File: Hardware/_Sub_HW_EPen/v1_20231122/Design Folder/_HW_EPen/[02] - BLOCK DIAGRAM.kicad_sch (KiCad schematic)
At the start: 0 parts

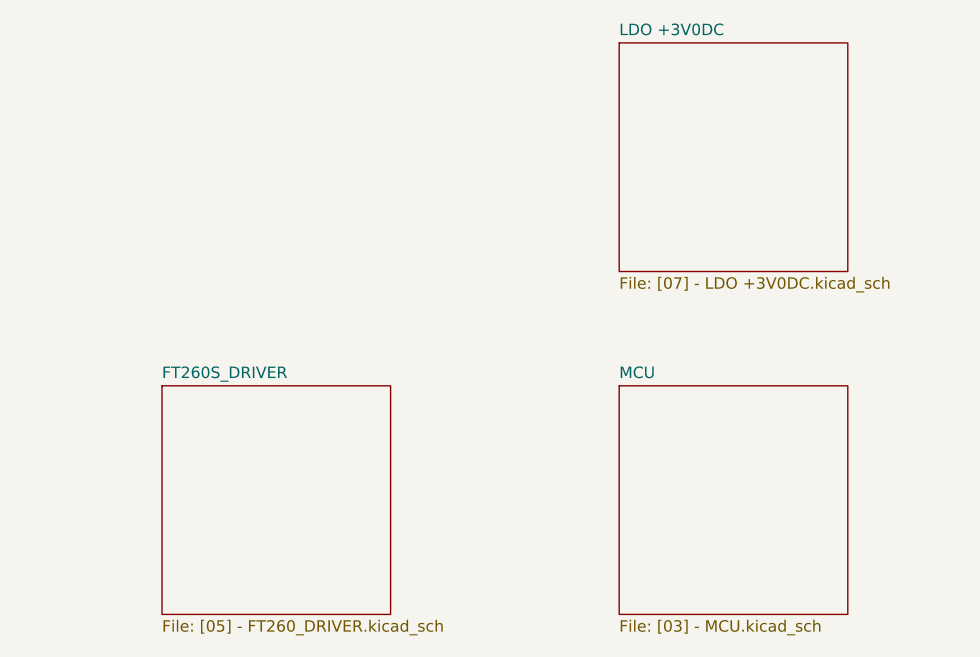
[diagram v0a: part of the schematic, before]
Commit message: Working on EPen schematic
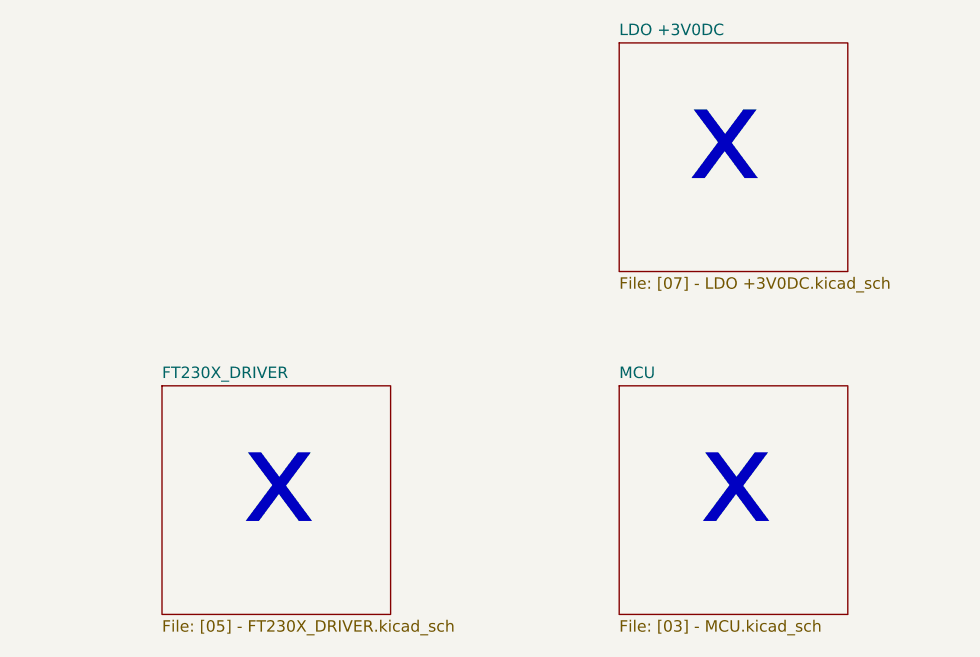
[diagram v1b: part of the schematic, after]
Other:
- sheet FT260S_DRIVER renamed FT230X_DRIVER
- sheet FT230X_DRIVER: file [05] - FT260_DRIVER.kicad_sch -> [05] - FT230X_DRIVER.kicad_sch
- note added: "x"
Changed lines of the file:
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@@
 (kicad_sch (version 20230121) (generator eeschema)
   (paper "B")
+  (text "x" (at 199.39 143.51 0)
+    (effects (font (size 10.16 10.16)) (justify left bottom))
+  )
+  (text "x" (at 148.59 143.51 0)
+    (effects (font (size 10.16 10.16)) (justify left bottom))
+  )
+  (text "x" (at 198.12 105.41 0)
+    (effects (font (size 10.16 10.16)) (justify left bottom))
+  )
   (sheet (at 88.9 127) (size 25.4 25.4) (fields_autoplaced)
     (stroke (width 0.1524) (type solid))
@@
     (stroke (width 0.1524) (type solid))
     (fill (color 0 0 0 0.0000))
-    (property "Sheetname" "FT260S_DRIVER" (at 139.7 126.2884 0)
+    (property "Sheetname" "FT230X_DRIVER" (at 139.7 126.2884 0)
       (effects (font (size 1.27 1.27)) (justify left bottom))
     )
-    (property "Sheetfile" "[05] - FT260_DRIVER.kicad_sch" (at 139.7 152.9846 0)
+    (property "Sheetfile" "[05] - FT230X_DRIVER.kicad_sch" (at 139.7 152.9846 0)
       (effects (font (size 1.27 1.27)) (justify left top))
     )

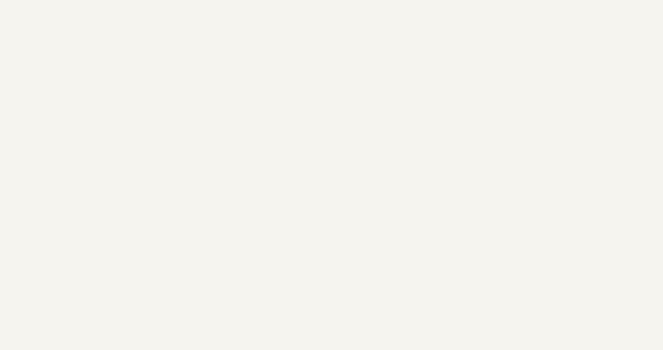
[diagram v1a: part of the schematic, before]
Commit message: Working on EPen schematic
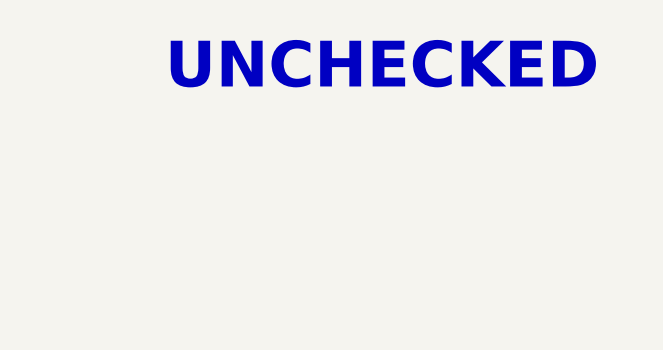
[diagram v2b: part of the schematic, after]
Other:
- note added: "UNCHECKED"
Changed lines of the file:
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@@
 (kicad_sch (version 20230121) (generator eeschema)
   (paper "B")
+  (text "UNCHECKED" (at 369.57 36.83 0)
+    (effects (font (size 5.08 5.08) (thickness 1.016) bold) (justify left bottom))
+  )
   (text "x" (at 199.39 143.51 0)
     (effects (font (size 10.16 10.16)) (justify left bottom))

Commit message: Working on Epen Schematic
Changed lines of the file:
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@@
     (effects (font (size 5.08 5.08) (thickness 1.016) bold) (justify left bottom))
   )
-  (text "x" (at 199.39 143.51 0)
+  (text "x" (at 248.92 143.51 0)
     (effects (font (size 10.16 10.16)) (justify left bottom))
   )
@@
     (effects (font (size 10.16 10.16)) (justify left bottom))
   )
+  (text "x" (at 96.52 143.51 0)
+    (effects (font (size 10.16 10.16)) (justify left bottom))
+  )

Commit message: More progress on EPen Hardware
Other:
- sheet FT230X_DRIVER ports: added UART_RX, UART_TX, USBDM, USBDP, VIN; removed none
- sheet LDO +3V0DC ports: added +3VOUT, MIC5365_EN, VIN; removed none
- sheet MCU ports: added BUFF_~{EN}, EEPROM_~{WP}, MCU_~{RESET}, MIC5365_EN, SPI_CLK, SPI_CS, SPI_MISO, SPI_MOSI, UART_RX, UART_TX, VIN; removed none
- sheet OUTPUT ports: added A1, A2, A4, A5, A6, VIN, Y3, ~{EN}; removed none
- sheet USB ports: added USBDM, USBDP, VBUS; removed none
- note removed: "UNCHECKED"
- note removed: "x"
- company: (none) -> mend0z0
- title: (none) -> EPen
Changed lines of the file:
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@@
 (kicad_sch (version 20230121) (generator eeschema)
   (paper "B")
-  (text "UNCHECKED" (at 369.57 36.83 0)
-    (effects (font (size 5.08 5.08) (thickness 1.016) bold) (justify left bottom))
-  )
-  (text "x" (at 248.92 143.51 0)
-    (effects (font (size 10.16 10.16)) (justify left bottom))
-  )
-  (text "x" (at 148.59 143.51 0)
-    (effects (font (size 10.16 10.16)) (justify left bottom))
-  )
-  (text "x" (at 198.12 105.41 0)
-    (effects (font (size 10.16 10.16)) (justify left bottom))
-  )
-  (text "x" (at 96.52 143.51 0)
-    (effects (font (size 10.16 10.16)) (justify left bottom))
+  (title_block
+    (title "EPen")
+    (date "2023-11-27")
+    (rev "v1.0")
+    (company "mend0z0")
+    (comment 1 "v1.0")
+    (comment 2 "PRELIMINARY")
+    (comment 4 "_BOM_EPen.html")
+    (comment 5 "_HW_EPen.pcb")
+    (comment 6 "_GBR_EPen.zip")
+    (comment 7 "_BOM_EPen.html")
+    (comment 9 "First Release")
+  )
+  (junction (at 177.8 93.98) (diameter 0) (color 0 0 0 0)
+  )
+  (junction (at 127 130.81) (diameter 0) (color 0 0 0 0)
+  )
+  (wire (pts (xy 215.9 138.43) (xy 266.7 138.43))
+    (stroke (width 0) (type default))
+  )
+  (wire (pts (xy 215.9 140.97) (xy 266.7 140.97))
+    (stroke (width 0) (type default))
+  )
+  (wire (pts (xy 222.25 129.54) (xy 222.25 106.68))
+    (stroke (width 0) (type default))
+  )
+  (wire (pts (xy 114.3 138.43) (xy 139.7 138.43))
+    (stroke (width 0) (type default))
+  )
+  (wire (pts (xy 190.5 129.54) (xy 177.8 129.54))
+    (stroke (width 0) (type default))
+  )
+  (wire (pts (xy 127 130.81) (xy 139.7 130.81))
+    (stroke (width 0) (type default))
+  )
+  (wire (pts (xy 215.9 135.89) (xy 266.7 135.89))
+    (stroke (width 0) (type default))
+  )
+  (wire (pts (xy 165.1 140.97) (xy 190.5 140.97))
+    (stroke (width 0) (type default))
+  )
+  (wire (pts (xy 177.8 129.54) (xy 177.8 93.98))
+    (stroke (width 0) (type default))
+  )
+  (wire (pts (xy 165.1 138.43) (xy 190.5 138.43))
+    (stroke (width 0) (type default))
+  )
+  (wire (pts (xy 215.9 143.51) (xy 266.7 143.51))
+    (stroke (width 0) (type default))
+  )
+  (wire (pts (xy 114.3 140.97) (xy 139.7 140.97))
+    (stroke (width 0) (type default))
+  )
+  (wire (pts (xy 114.3 130.81) (xy 127 130.81))
+    (stroke (width 0) (type default))
+  )
+  (wire (pts (xy 215.9 129.54) (xy 222.25 129.54))
+    (stroke (width 0) (type default))
+  )
+  (wire (pts (xy 228.6 93.98) (xy 177.8 93.98))
+    (stroke (width 0) (type default))
+  )
+  (wire (pts (xy 215.9 149.86) (xy 266.7 149.86))
+    (stroke (width 0) (type default))
+  )
+  (wire (pts (xy 127 93.98) (xy 127 130.81))
+    (stroke (width 0) (type default))
+  )
+  (wire (pts (xy 260.35 95.25) (xy 260.35 129.54))
+    (stroke (width 0) (type default))
+  )
+  (wire (pts (xy 222.25 106.68) (xy 228.6 106.68))
+    (stroke (width 0) (type default))
+  )
+  (wire (pts (xy 260.35 129.54) (xy 266.7 129.54))
+    (stroke (width 0) (type default))
+  )
+  (wire (pts (xy 215.9 146.05) (xy 266.7 146.05))
+    (stroke (width 0) (type default))
+  )
+  (wire (pts (xy 254 95.25) (xy 260.35 95.25))
+    (stroke (width 0) (type default))
+  )
+  (wire (pts (xy 177.8 93.98) (xy 127 93.98))
+    (stroke (width 0) (type default))
+  )
+  (wire (pts (xy 215.9 133.35) (xy 266.7 133.35))
+    (stroke (width 0) (type default))
   )
   (sheet (at 88.9 127) (size 25.4 25.4) (fields_autoplaced)
@@
       (effects (font (size 1.27 1.27)) (justify left top))
     )
+    (pin "USBDP" bidirectional (at 114.3 140.97 0)
+      (effects (font (size 1.27 1.27)) (justify right))
+    )
+    (pin "USBDM" bidirectional (at 114.3 138.43 0)
+      (effects (font (size 1.27 1.27)) (justify right))
+    )
+    (pin "VBUS" output (at 114.3 130.81 0)
+      (effects (font (size 1.27 1.27)) (justify right))
+    )
     (instances
       (project "_HW_EPen"
@@
       (effects (font (size 1.27 1.27)) (justify left top))
     )
+    (pin "VIN" input (at 190.5 129.54 180)
+      (effects (font (size 1.27 1.27)) (justify left))
+    )
+    (pin "SPI_CLK" output (at 215.9 140.97 0)
+      (effects (font (size 1.27 1.27)) (justify right))
+    )
+    (pin "SPI_CS" output (at 215.9 135.89 0)
+      (effects (font (size 1.27 1.27)) (justify right))
+    )
+    (pin "UART_RX" input (at 190.5 138.43 180)
+      (effects (font (size 1.27 1.27)) (justify left))
+    )
+    (pin "UART_TX" output (at 190.5 140.97 180)
+      (effects (font (size 1.27 1.27)) (justify left))
+    )
+    (pin "SPI_MOSI" output (at 215.9 138.43 0)
+      (effects (font (size 1.27 1.27)) (justify right))
+    )
+    (pin "MIC5365_EN" output (at 215.9 129.54 0)
+      (effects (font (size 1.27 1.27)) (justify right))
+    )
+    (pin "BUFF_~{EN}" output (at 215.9 133.35 0)
+      (effects (font (size 1.27 1.27)) (justify right))
+    )
+    (pin "MCU_~{RESET}" output (at 215.9 146.05 0)
+      (effects (font (size 1.27 1.27)) (justify right))
+    )
+    (pin "EEPROM_~{WP}" output (at 215.9 143.51 0)
+      (effects (font (size 1.27 1.27)) (justify right))
+    )
+    (pin "SPI_MISO" input (at 215.9 149.86 0)
+      (effects (font (size 1.27 1.27)) (justify right))
+    )
     (instances
       (project "_HW_EPen"
@@
     )
   )
-  (sheet (at 241.3 127) (size 25.4 25.4) (fields_autoplaced)
-    (stroke (width 0.1524) (type solid))
-    (fill (color 0 0 0 0.0000))
-    (property "Sheetname" "OUTPUT" (at 241.3 126.2884 0)
-      (effects (font (size 1.27 1.27)) (justify left bottom))
-    )
-    (property "Sheetfile" "[04] - OUTPUT.kicad_sch" (at 241.3 152.9846 0)
-      (effects (font (size 1.27 1.27)) (justify left top))
+  (sheet (at 266.7 127) (size 25.4 25.4) (fields_autoplaced)
+    (stroke (width 0.1524) (type solid))
+    (fill (color 0 0 0 0.0000))
+    (property "Sheetname" "OUTPUT" (at 266.7 126.2884 0)
+      (effects (font (size 1.27 1.27)) (justify left bottom))
+    )
+    (property "Sheetfile" "[04] - OUTPUT.kicad_sch" (at 266.7 152.9846 0)
+      (effects (font (size 1.27 1.27)) (justify left top))
+    )
+    (pin "VIN" input (at 266.7 129.54 180)
+      (effects (font (size 1.27 1.27)) (justify left))
+    )
+    (pin "A6" input (at 266.7 146.05 180)
+      (effects (font (size 1.27 1.27)) (justify left))
+    )
+    (pin "A5" input (at 266.7 143.51 180)
+      (effects (font (size 1.27 1.27)) (justify left))
+    )
+    (pin "A4" input (at 266.7 140.97 180)
+      (effects (font (size 1.27 1.27)) (justify left))
+    )
+    (pin "~{EN}" input (at 266.7 133.35 180)
+      (effects (font (size 1.27 1.27)) (justify left))
+    )
+    (pin "A1" input (at 266.7 135.89 180)
+      (effects (font (size 1.27 1.27)) (justify left))
+    )
+    (pin "A2" input (at 266.7 138.43 180)
+      (effects (font (size 1.27 1.27)) (justify left))
+    )
+    (pin "Y3" output (at 266.7 149.86 180)
+      (effects (font (size 1.27 1.27)) (justify left))
     )
     (instances
@@
       (effects (font (size 1.27 1.27)) (justify left top))
     )
+    (pin "VIN" input (at 139.7 130.81 180)
+      (effects (font (size 1.27 1.27)) (justify left))
+    )
+    (pin "USBDM" bidirectional (at 139.7 138.43 180)
+      (effects (font (size 1.27 1.27)) (justify left))
+    )
+    (pin "USBDP" bidirectional (at 139.7 140.97 180)
+      (effects (font (size 1.27 1.27)) (justify left))
+    )
+    (pin "UART_TX" output (at 165.1 138.43 0)
+      (effects (font (size 1.27 1.27)) (justify right))
+    )
+    (pin "UART_RX" input (at 165.1 140.97 0)
+      (effects (font (size 1.27 1.27)) (justify right))
+    )
     (instances
       (project "_HW_EPen"
@@
     )
   )
-  (sheet (at 190.5 88.9) (size 25.4 25.4) (fields_autoplaced)
-    (stroke (width 0.1524) (type solid))
-    (fill (color 0 0 0 0.0000))
-    (property "Sheetname" "LDO +3V0DC" (at 190.5 88.1884 0)
-      (effects (font (size 1.27 1.27)) (justify left bottom))
-    )
-    (property "Sheetfile" "[07] - LDO +3V0DC.kicad_sch" (at 190.5 114.8846 0)
-      (effects (font (size 1.27 1.27)) (justify left top))
-    )
-    (instances
+  (sheet (at 228.6 88.9) (size 25.4 25.4) (fields_autoplaced)
+    (stroke (width 0.1524) (type solid))
+    (fill (color 0 0 0 0.0000))
+    (property "Sheetname" "LDO +3V0DC" (at 228.6 88.1884 0)
+      (effects (font (size 1.27 1.27)) (justify left bottom))
+    )
+    (property "Sheetfile" "[07] - LDO +3V0DC.kicad_sch" (at 228.6 114.8846 0)
+      (effects (font (size 1.27 1.27)) (justify left top))
+    )
+    (pin "MIC5365_EN" input (at 228.6 106.68 180)
+      (effects (font (size 1.27 1.27)) (justify left))
+    )
+    (pin "VIN" input (at 228.6 93.98 180)
+      (effects (font (size 1.27 1.27)) (justify left))
+    )
+    (pin "+3VOUT" output (at 254 95.25 0)
+      (effects (font (size 1.27 1.27)) (justify right))
+    )
+    (instances

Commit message: _HW_EPen is ready to be worked for layout
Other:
- title: EPen -> _HW_EPen
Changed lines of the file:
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@@
   (paper "B")
   (title_block
-    (title "EPen")
+    (title "_HW_EPen")
     (date "2023-11-27")
     (rev "v1.0")
     (company "mend0z0")
     (comment 1 "v1.0")
-    (comment 2 "PRELIMINARY")
+    (comment 2 "CHECKED")
     (comment 4 "_BOM_EPen.html")
     (comment 5 "_HW_EPen.pcb")
     (comment 6 "_GBR_EPen.zip")
     (comment 7 "_BOM_EPen.html")
+    (comment 8 "N/A")
     (comment 9 "First Release")
   )
